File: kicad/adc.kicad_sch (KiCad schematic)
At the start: 11 parts, among them U1 AD7606BBSTZ-RL

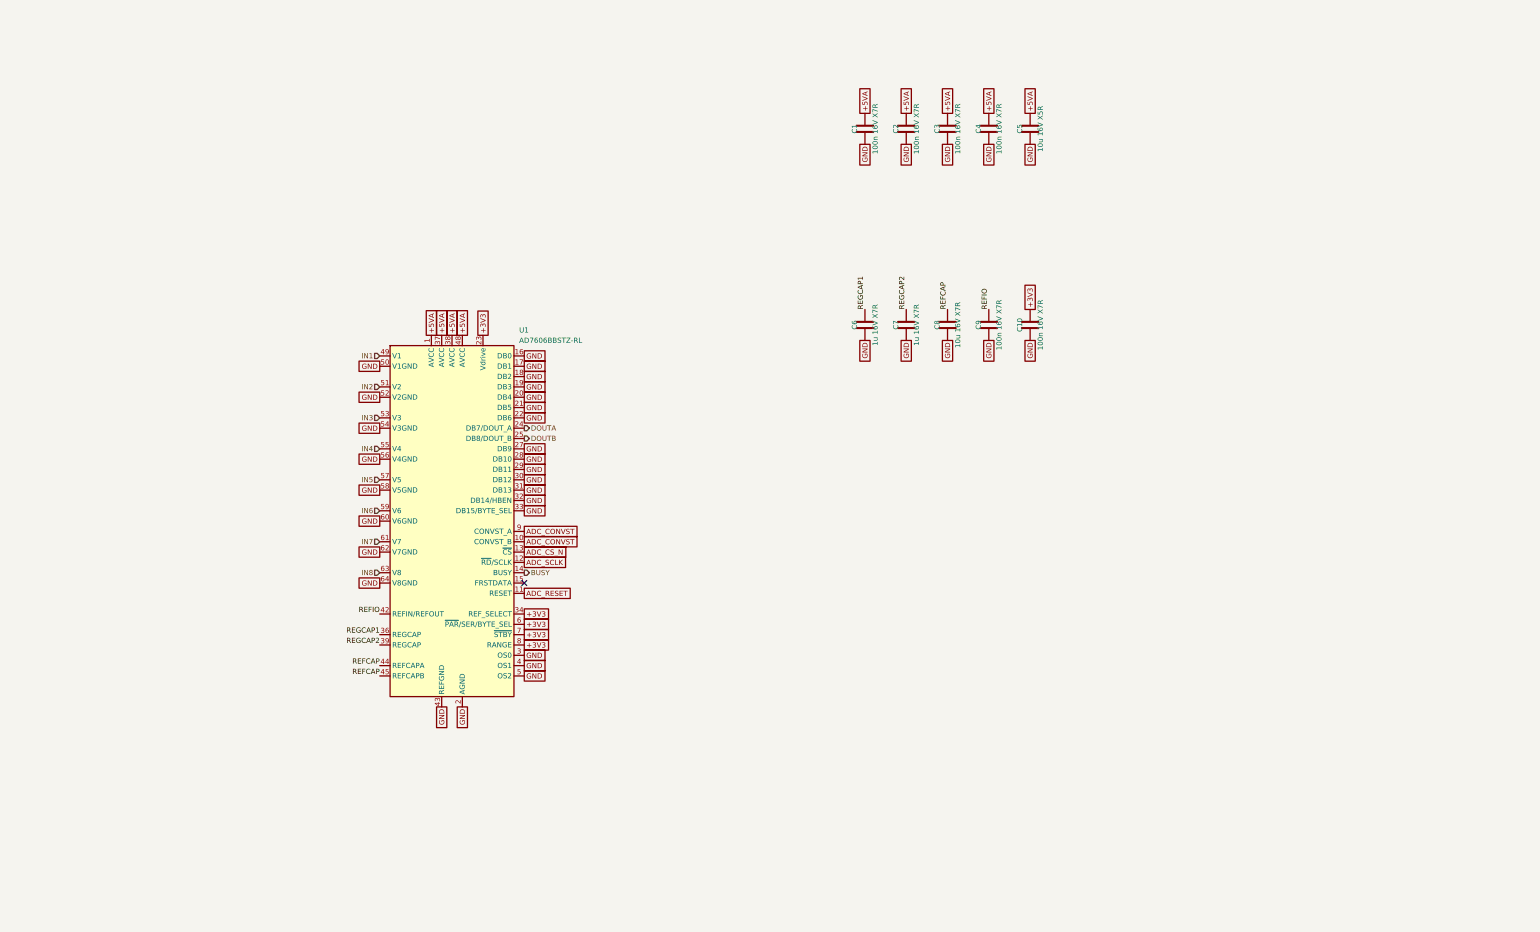
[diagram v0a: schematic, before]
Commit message: AD7606C-16, one sheet per repeated block, clock buffering, first simulations
- ADC: AD7606C-16 in software mode (OS pins high, WR held high, DB11/SDI on
  shared ADC_SDI), 33 R source resistors on DOUTA/DOUTB/BUSY.
- Every repeated block is its own reused sheet: tx_group x16, en_buf x4,
  clk_buf x7, mic x8 (replaces tx_shift, tx_drivers, mems). Sheets other than
  channel are generated by scripts/build_cells.py and scripts/build_power.py.
- Headers: GND conductors either side of every clock, ADC_SDI, idle pulls,
  DNP RC terminations as fallback.
- Power: 3V3_MIC ferrite filter moved to the power sheet with LED, test point
  and flag.
- Simulations (LTspice, sim/): RX chain gain/noise, TX burst and recovery,
  clock signal integrity; results in docs/simulation-1.md. FPGA ribbon outputs
  changed to DRIVE 4 after simulation.
- Brief, CLAUDE.md, review status and SKiDL reference spec updated.
  ERC: 0 violations, 1,701 parts.
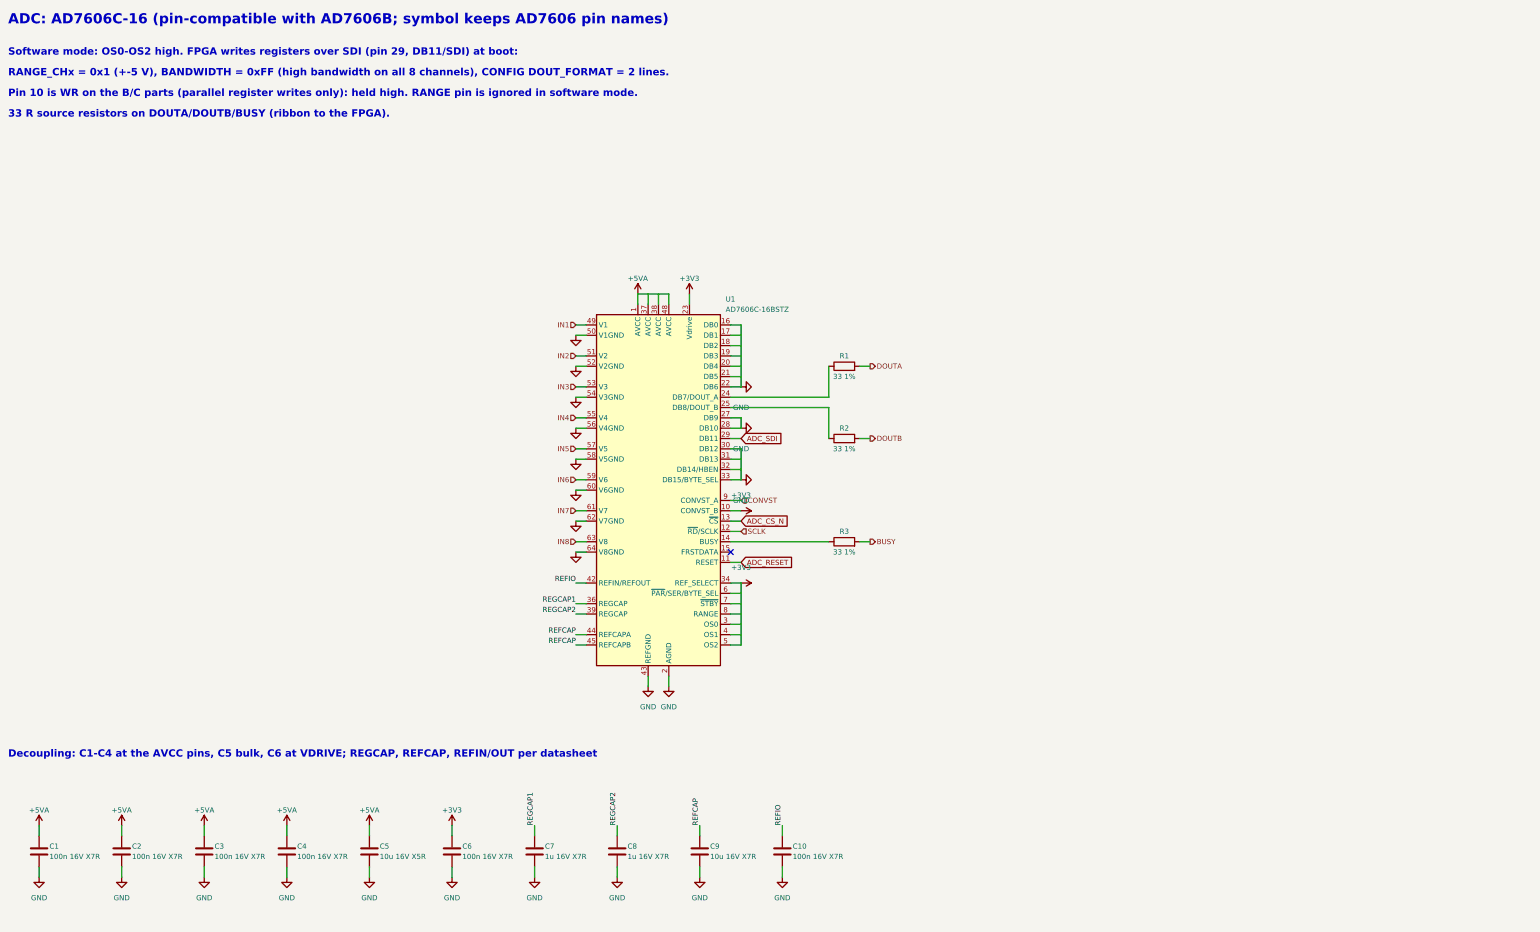
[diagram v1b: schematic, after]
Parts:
- added R1, R2, R3: 33 1%, Resistor_SMD:R_0603_1608Metric, symbol Device:R
- C6: value 1u 16V X7R -> 100n 16V X7R
- C8: value 10u 16V X7R -> 1u 16V X7R; footprint Capacitor_SMD:C_1206_3216Metric -> Capacitor_SMD:C_0603_1608Metric
- C9: value 100n 16V X7R -> 10u 16V X7R; footprint Capacitor_SMD:C_0603_1608Metric -> Capacitor_SMD:C_1206_3216Metric
- U1: value AD7606BBSTZ-RL -> AD7606C-16BSTZ; LCSC C651284 -> consigned (DigiKey/Mouser, not on LCSC)
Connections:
- net +3V3: now also C6.1, U1.10 (CONVST_B), U1.3 (OS0), U1.4 (OS1), U1.5 (OS2); no longer C10.1
- net BUSY: now also R3.2; no longer U1.14 (BUSY)
- net DOUTA: now also R1.2; no longer U1.24 (DB7/DOUT_A)
- net DOUTB: now also R2.2; no longer U1.25 (DB8/DOUT_B)
- net GND: no longer U1.29 (DB11), U1.3 (OS0), U1.4 (OS1), U1.5 (OS2)
- net REFCAP: now also C9.1; no longer C8.1
- net REFIO: now also C10.1; no longer C9.1
- net REGCAP1: now also C7.1; no longer C6.1
- net REGCAP2: now also C8.1; no longer C7.1
- net ADC_CONVST renamed CONVST
- net CONVST: no longer U1.10 (CONVST_B)
- net ADC_SCLK renamed SCLK
- new net: R3.1, U1.14 (BUSY)
- new net: R2.1, U1.25 (DB8/DOUT_B)
- new net: R1.1, U1.24 (DB7/DOUT_A)
- new net ADC_SDI: U1.29 (DB11)
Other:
- note added: "33 R source resistors on DOUTA/DOUTB/BUSY (ribbon to the FPGA)."
- note added: "ADC: AD7606C-16 (pin-compatible with AD7606B; symbol keeps AD7606 pin names)"
- note added: "Decoupling: C1-C4 at the AVCC pins, C5 bulk, C6 at VDRIVE; REGCAP, REFCAP, REFIN/OUT per datasheet"
- note added: "Pin 10 is WR on the B/C parts (parallel register writes only): held high. RANGE pin is ignored in software mode."
- note added: "RANGE_CHx = 0x1 (+-5 V), BANDWIDTH = 0xFF (high bandwidth on all 8 channels), CONFIG DOUT_FORMAT = 2 lines."
- note added: "Software mode: OS0-OS2 high. FPGA writes registers over SDI (pin 29, DB11/SDI) at boot:"

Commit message: Block-diagram top page, power review fixes, readable sheets
Top level
- Page 1 is now a block diagram of the signal flow (FPGA -> headers ->
  clock buffers / TX drive -> transceivers -> ADCs -> FPGA, mics, power).
- New group sheets hold the reused cells: tx (16 tx_group + 4 en_buf),
  array (64 channel), adcs (8 adc), mics (8 mic), clocks (7 clk_buf).
  Power and headers stay directly under the top. All written by gen_top.py,
  which now also survives a kicad-cli re-save of a cell sheet.

Power (review findings)
- Polyfuse 1812L200/16DR (16 V), TPS65131RGER stated explicitly, input caps
  2 x 10u 1206, 50 V caps on 12 V, inductor values carry minimum Isat.
- +3V3: TLV75733P (ceramic-stable) replaces TLV1117-33.
- New JP5/JP6 isolate +-6V5; every rail: REG node -> jumper -> rail with TP,
  LED (not on analog LDOs) and PWR_FLAG.
- Power sheet is now generated by build_cells.py in a 2x3 block layout
  (build_power.py removed).

Readability and small fixes
- Rails on sideways pins use labelled flags; sideways GND symbols hide text.
- tx_group: 595 outputs wired straight to the drivers.
- Title blocks on every sheet; channel sheet notes and field placement fixed
  (sch_fields.py --only, sch_annotate.py).
- ADC_SDI 10k pull-down, ADC reset/DOUT notes, mic cap 50 V.
- ERC 0 violations, 1,704 parts. PDFs: docs/schematics/00..13.
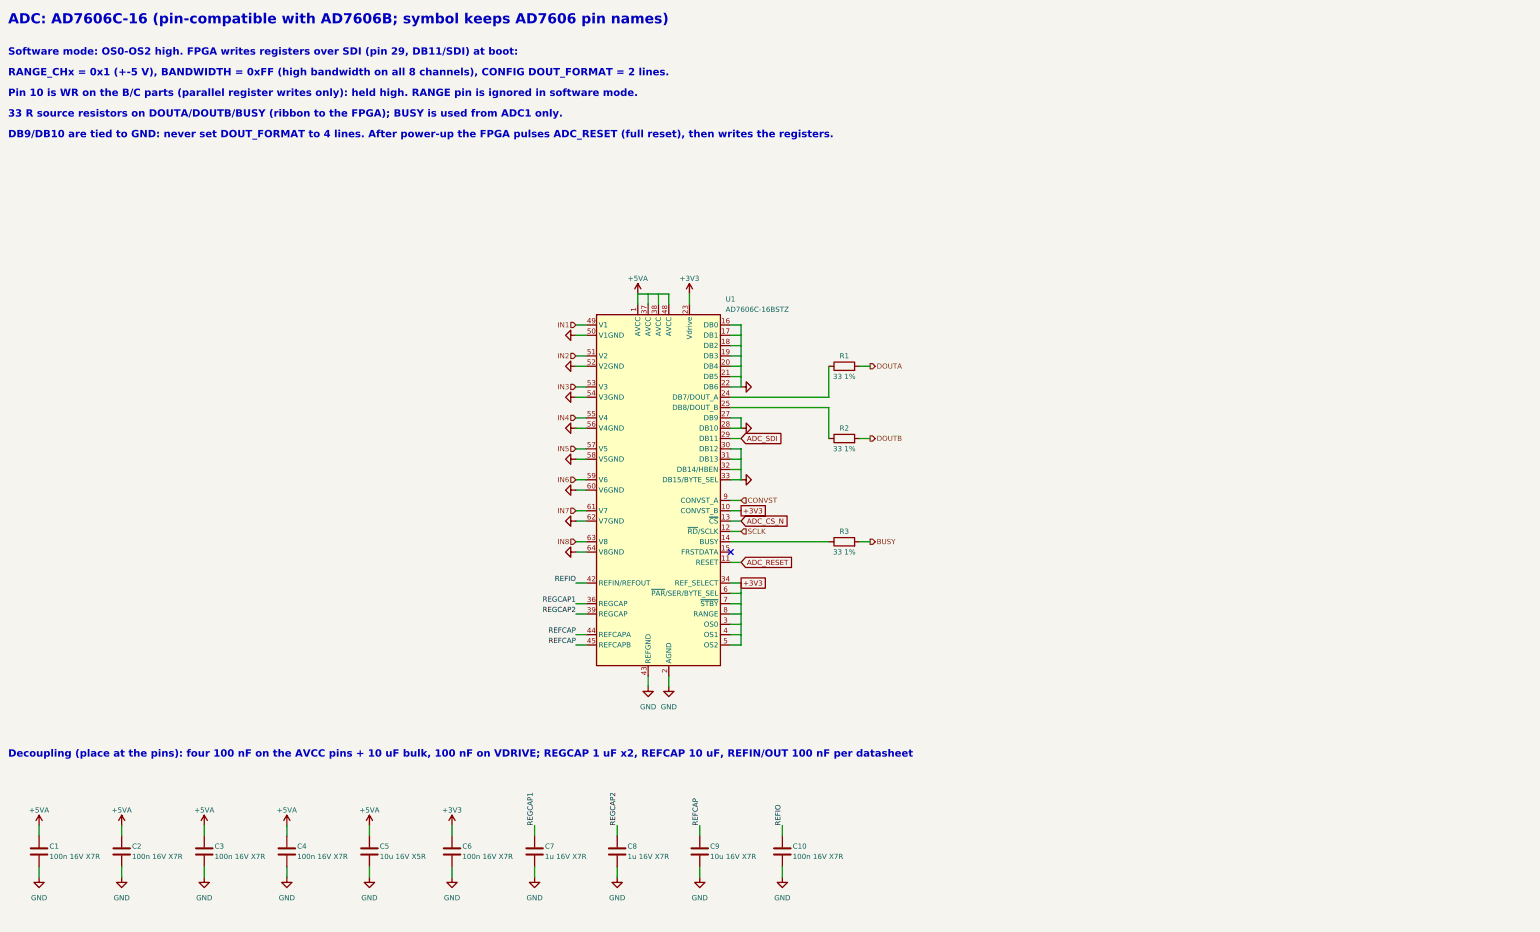
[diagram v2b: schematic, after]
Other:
- note added: "33 R source resistors on DOUTA/DOUTB/BUSY (ribbon to the FPGA); BUSY is used from ADC1 only."
- note added: "DB9/DB10 are tied to GND: never set DOUT_FORMAT to 4 lines. After power-up the FPGA pulses ADC_RESET (full reset), then writes the registers."
- note added: "Decoupling (place at the pins): four 100 nF on the AVCC pins + 10 uF bulk, 100 nF on VDRIVE; REGCAP 1 uF x2, REFCAP 10 uF, REFIN/OUT 100 nF per datasheet"
- note removed: "33 R source resistors on DOUTA/DOUTB/BUSY (ribbon to the FPGA)."
- note removed: "Decoupling: C1-C4 at the AVCC pins, C5 bulk, C6 at VDRIVE; REGCAP, REFCAP, REFIN/OUT per datasheet"
- company: (none) -> Hybrid 8x8 ultrasonic AESA
- title: (none) -> ADC (x8): AD7606C-16, software mode, serial 2 DOUT

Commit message: Optimized, costed BOM with LCSC numbers for every part
scripts/bom.py picks parts (Basic first, stock margin) and writes docs/bom.md,
fab/bom_jlcpcb.csv and scripts/parts.json; sch_lcsc.py fills LCSC fields from it.
Part changes: TPS7A4700RGWT for the out-of-stock TPS7A4701, BAV99 C2500, SS54 in SMA,
SMD1812P200TF16 polyfuse, 600R ferrite, Basic-value +5V/VDRV dividers (VDRV 15.4 V),
Sunlord SWPA6045 footprints, mic 100 nF C0G in 1206. AD7606C-16 and SPH0641 now
assembled by JLCPCB.
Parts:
- C1, C10, C2, C3, C4, C6: LCSC TBD -> C14663
- C5: LCSC TBD -> C15850
- C7, C8: LCSC TBD -> C388002
- C9: LCSC TBD -> C380363
- R1, R2, R3: LCSC TBD -> C23140
- U1: LCSC consigned (DigiKey/Mouser, not on LCSC) -> C5240947
